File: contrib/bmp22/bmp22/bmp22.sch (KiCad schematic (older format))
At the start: 2 parts, among them U101 LP2985-3.3

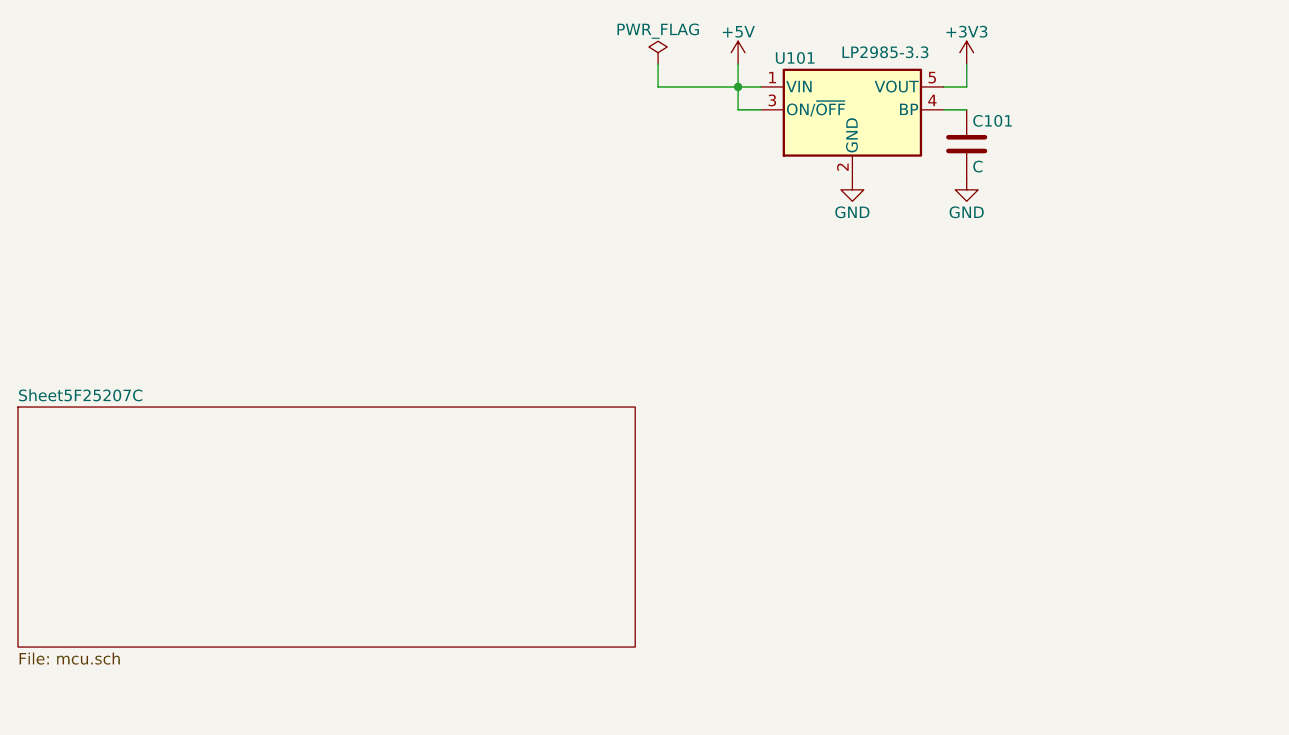
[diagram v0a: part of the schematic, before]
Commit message: added footprints
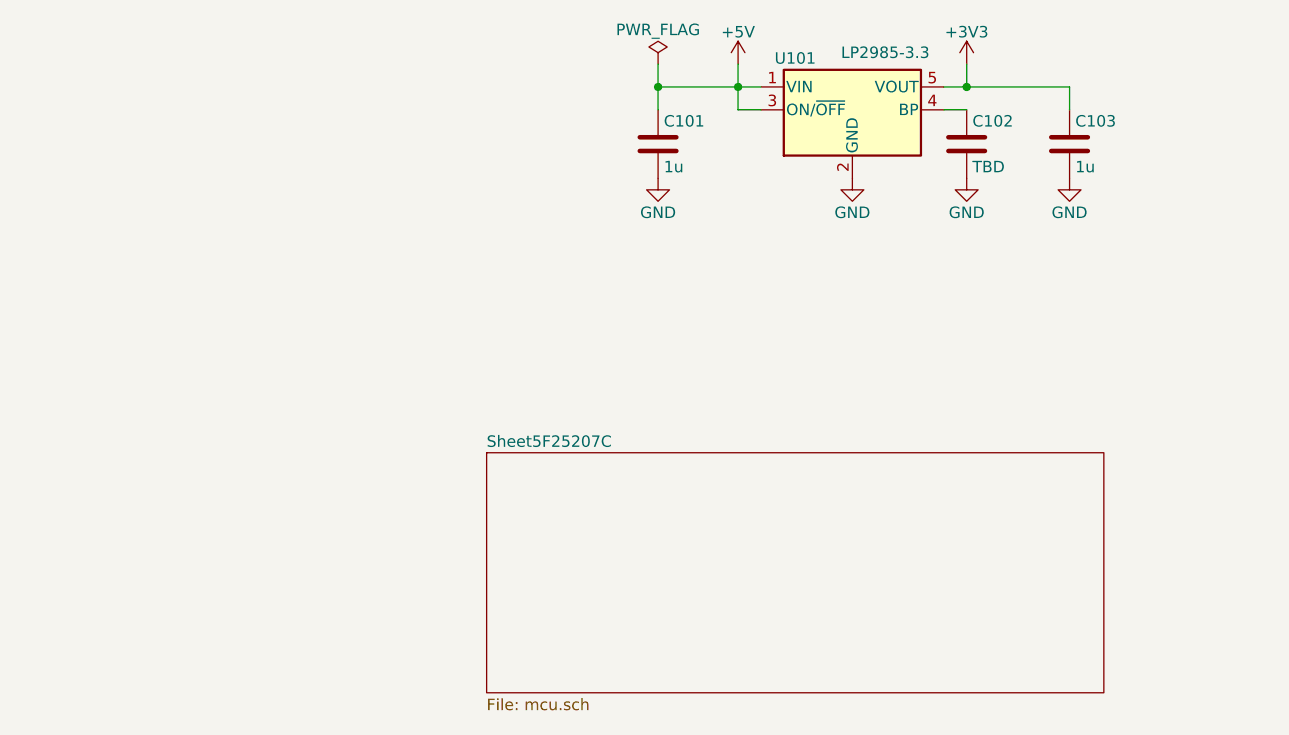
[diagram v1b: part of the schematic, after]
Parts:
- added C101, C103: 1u, Capacitor_SMD:C_0603_1608Metric, symbol Device:C
- C102: renamed from C101; value C -> TBD; footprint (none) -> Capacitor_SMD:C_0603_1608Metric
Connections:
- net +3V3: now also C103.1
- net +5V: now also C101.1
- net GND: now also C101.2, C103.2
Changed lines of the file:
@@
 $EndSheet
 $Sheet
-S 1600 2850 2700 1050
+S 3650 3050 2700 1050
 U 5F25207D
 F0 "Sheet5F25207C" 50
@@
 $EndComp
 $Comp
-L power:GND #PWR0178
+L power:GND #PWR0104
 U 1 1 5F42B067
 P 5250 1850
-F 0 "#PWR0178" H 5250 1600 50  0001 C CNN
+F 0 "#PWR0104" H 5250 1600 50  0001 C CNN
 F 1 "GND" H 5250 1700 50  0000 C CNN
 F 2 "" H 5250 1850 50  0001 C CNN
@@
 $EndComp
 $Comp
-L Device:C C101
+L Device:C C102
 U 1 1 5F42B588
 P 5750 1700
-F 0 "C101" H 5775 1800 50  0000 L CNN
-F 1 "C" H 5775 1600 50  0000 L CNN
-F 2 "" H 5788 1550 50  0001 C CNN
+F 0 "C102" H 5775 1800 50  0000 L CNN
+F 1 "TBD" H 5775 1600 50  0000 L CNN
+F 2 "Capacitor_SMD:C_0603_1608Metric" H 5788 1550 50  0001 C CNN
 F 3 "~" H 5750 1700 50  0001 C CNN
 	1    5750 1700
@@
 	5750 1550 5650 1550
 $Comp
-L power:GND #PWR0179
+L power:GND #PWR0105
 U 1 1 5F42BA16
 P 5750 1850
-F 0 "#PWR0179" H 5750 1600 50  0001 C CNN
+F 0 "#PWR0105" H 5750 1600 50  0001 C CNN
 F 1 "GND" H 5750 1700 50  0000 C CNN
 F 2 "" H 5750 1850 50  0001 C CNN
@@
 	4750 1450 4850 1450
 $Comp
-L power:+5V #PWR0176
+L power:+5V #PWR0101
 U 1 1 5F42C346
 P 4750 1350
-F 0 "#PWR0176" H 4750 1200 50  0001 C CNN
+F 0 "#PWR0101" H 4750 1200 50  0001 C CNN
 F 1 "+5V" H 4750 1490 50  0000 C CNN
 F 2 "" H 4750 1350 50  0001 C CNN
@@
 Connection ~ 4750 1450
 $Comp
-L power:+3V3 #PWR0177
+L power:+3V3 #PWR0102
 U 1 1 5F42CC0D
 P 5750 1350
-F 0 "#PWR0177" H 5750 1200 50  0001 C CNN
+F 0 "#PWR0102" H 5750 1200 50  0001 C CNN
 F 1 "+3V3" H 5750 1490 50  0000 C CNN
 F 2 "" H 5750 1350 50  0001 C CNN
@@
 Wire Wire Line
 	4400 1450 4750 1450
+$Comp
+L Device:C C103
+U 1 1 5F483C75
+P 6200 1700
+F 0 "C103" H 6225 1800 50  0000 L CNN
+F 1 "1u" H 6225 1600 50  0000 L CNN
+F 2 "Capacitor_SMD:C_0603_1608Metric" H 6238 1550 50  0001 C CNN
+F 3 "~" H 6200 1700 50  0001 C CNN
+	1    6200 1700
+	1    0    0    -1
+$EndComp
+$Comp
+L power:GND #PWR0106
+U 1 1 5F483FBC
+P 6200 1850
+F 0 "#PWR0106" H 6200 1600 50  0001 C CNN
+F 1 "GND" H 6200 1700 50  0000 C CNN
+F 2 "" H 6200 1850 50  0001 C CNN
+F 3 "" H 6200 1850 50  0001 C CNN
+	1    6200 1850
+	1    0    0    -1
+$EndComp
+Wire Wire Line
+	6200 1550 6200 1450
+Wire Wire Line
+	6200 1450 5750 1450
+Connection ~ 5750 1450
+$Comp
+L Device:C C101
+U 1 1 5F48509D
+P 4400 1700
+F 0 "C101" H 4425 1800 50  0000 L CNN
+F 1 "1u" H 4425 1600 50  0000 L CNN
+F 2 "Capacitor_SMD:C_0603_1608Metric" H 4438 1550 50  0001 C CNN
+F 3 "~" H 4400 1700 50  0001 C CNN
+	1    4400 1700
+	1    0    0    -1
+$EndComp
+$Comp
+L power:GND #PWR0103
+U 1 1 5F4850A3
+P 4400 1850
+F 0 "#PWR0103" H 4400 1600 50  0001 C CNN
+F 1 "GND" H 4400 1700 50  0000 C CNN
+F 2 "" H 4400 1850 50  0001 C CNN
+F 3 "" H 4400 1850 50  0001 C CNN
+	1    4400 1850
+	1    0    0    -1
+$EndComp
+Wire Wire Line
+	4400 1550 4400 1450
+Connection ~ 4400 1450
 $EndSCHEMATC

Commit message: created layout
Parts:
- added FID1, FID2, FID3, FID4, FID5, FID6: Fiducial, Fiducial:Fiducial_1mm_Mask2mm, symbol Mechanical:Fiducial
- added H1, H2, H3, H4: MountingHole, MountingHole:MountingHole_2.7mm_M2.5_DIN965, symbol Mechanical:MountingHole
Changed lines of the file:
@@
 	4400 1550 4400 1450
 Connection ~ 4400 1450
+$Comp
+L Mechanical:Fiducial FID1
+U 1 1 5F19E2A2
+P 2500 5000
+F 0 "FID1" H 2585 5046 50  0000 L CNN
+F 1 "Fiducial" H 2585 4955 50  0000 L CNN
+F 2 "Fiducial:Fiducial_1mm_Mask2mm" H 2500 5000 50  0001 C CNN
+F 3 "~" H 2500 5000 50  0001 C CNN
+	1    2500 5000
+	1    0    0    -1
+$EndComp
+$Comp
+L Mechanical:Fiducial FID2
+U 1 1 5F19E943
+P 2500 5250
+F 0 "FID2" H 2585 5296 50  0000 L CNN
+F 1 "Fiducial" H 2585 5205 50  0000 L CNN
+F 2 "Fiducial:Fiducial_1mm_Mask2mm" H 2500 5250 50  0001 C CNN
+F 3 "~" H 2500 5250 50  0001 C CNN
+	1    2500 5250
+	1    0    0    -1
+$EndComp
+$Comp
+L Mechanical:Fiducial FID3
+U 1 1 5F21FF18
+P 2500 5500
+F 0 "FID3" H 2585 5546 50  0000 L CNN
+F 1 "Fiducial" H 2585 5455 50  0000 L CNN
+F 2 "Fiducial:Fiducial_1mm_Mask2mm" H 2500 5500 50  0001 C CNN
+F 3 "~" H 2500 5500 50  0001 C CNN
+	1    2500 5500
+	1    0    0    -1
+$EndComp
+$Comp
+L Mechanical:Fiducial FID4
+U 1 1 5F220B5C
+P 3500 5000
+F 0 "FID4" H 3585 5046 50  0000 L CNN
+F 1 "Fiducial" H 3585 4955 50  0000 L CNN
+F 2 "Fiducial:Fiducial_1mm_Mask2mm" H 3500 5000 50  0001 C CNN
+F 3 "~" H 3500 5000 50  0001 C CNN
+	1    3500 5000
+	1    0    0    -1
+$EndComp
+$Comp
+L Mechanical:Fiducial FID5
+U 1 1 5F220B62
+P 3500 5250
+F 0 "FID5" H 3585 5296 50  0000 L CNN
+F 1 "Fiducial" H 3585 5205 50  0000 L CNN
+F 2 "Fiducial:Fiducial_1mm_Mask2mm" H 3500 5250 50  0001 C CNN
+F 3 "~" H 3500 5250 50  0001 C CNN
+	1    3500 5250
+	1    0    0    -1
+$EndComp
+$Comp
+L Mechanical:Fiducial FID6
+U 1 1 5F220B68
+P 3500 5500
+F 0 "FID6" H 3585 5546 50  0000 L CNN
+F 1 "Fiducial" H 3585 5455 50  0000 L CNN
+F 2 "Fiducial:Fiducial_1mm_Mask2mm" H 3500 5500 50  0001 C CNN
+F 3 "~" H 3500 5500 50  0001 C CNN
+	1    3500 5500
+	1    0    0    -1
+$EndComp
+$Comp
+L Mechanical:MountingHole H1
+U 1 1 5F2A39DC
+P 2500 6000
+F 0 "H1" H 2600 6046 50  0000 L CNN
+F 1 "MountingHole" H 2600 5955 50  0000 L CNN
+F 2 "MountingHole:MountingHole_2.7mm_M2.5_DIN965" H 2500 6000 50  0001 C CNN
+F 3 "~" H 2500 6000 50  0001 C CNN
+	1    2500 6000
+	1    0    0    -1
+$EndComp
+$Comp
+L Mechanical:MountingHole H2
+U 1 1 5F2A6C32
+P 2500 6200
+F 0 "H2" H 2600 6246 50  0000 L CNN
+F 1 "MountingHole" H 2600 6155 50  0000 L CNN
+F 2 "MountingHole:MountingHole_2.7mm_M2.5_DIN965" H 2500 6200 50  0001 C CNN
+F 3 "~" H 2500 6200 50  0001 C CNN
+	1    2500 6200
+	1    0    0    -1
+$EndComp
+$Comp
+L Mechanical:MountingHole H3
+U 1 1 5F2A75CA
+P 3500 6000
+F 0 "H3" H 3600 6046 50  0000 L CNN
+F 1 "MountingHole" H 3600 5955 50  0000 L CNN
+F 2 "MountingHole:MountingHole_2.7mm_M2.5_DIN965" H 3500 6000 50  0001 C CNN
+F 3 "~" H 3500 6000 50  0001 C CNN
+	1    3500 6000
+	1    0    0    -1
+$EndComp
+$Comp
+L Mechanical:MountingHole H4
+U 1 1 5F2A75D0
+P 3500 6200
+F 0 "H4" H 3600 6246 50  0000 L CNN
+F 1 "MountingHole" H 3600 6155 50  0000 L CNN
+F 2 "MountingHole:MountingHole_2.7mm_M2.5_DIN965" H 3500 6200 50  0001 C CNN
+F 3 "~" H 3500 6200 50  0001 C CNN
+	1    3500 6200
+	1    0    0    -1
+$EndComp
 $EndSCHEMATC
